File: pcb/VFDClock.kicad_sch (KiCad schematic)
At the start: 32 parts, among them J1 USB_C_Receptacle_USB2.0_16P, SW1 SW_SPST, SW2 SW_SPST, U1 SN74HC595PWR, U2 TBD62783AFWG, U3 TBD62783AFWG, U4 ESP32-S3-WROOM-1, U5 AMS1117-3.3, U6 AMS1117-1.5, U7 AMS1117

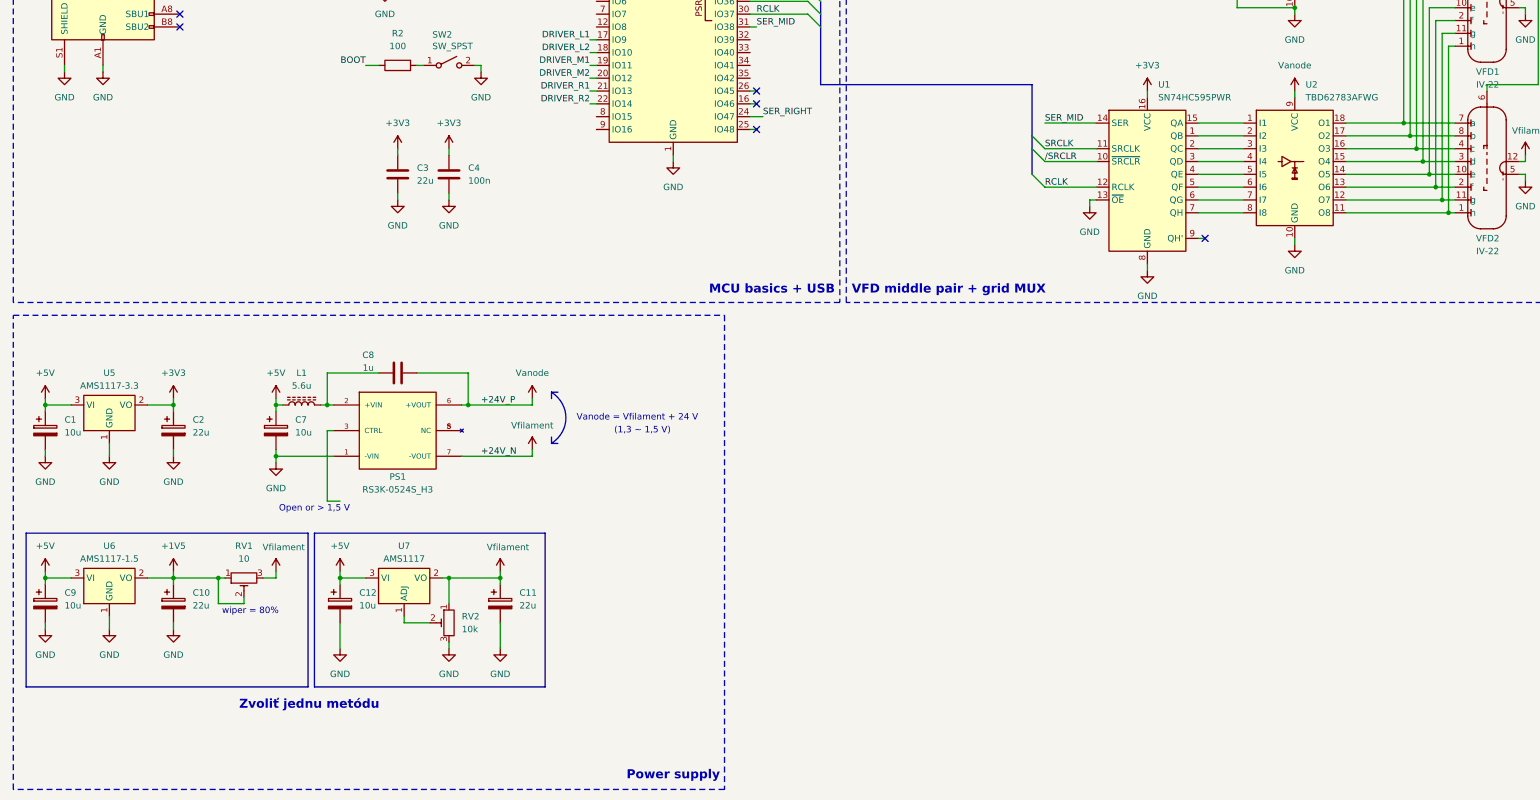
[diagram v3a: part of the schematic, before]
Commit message: Added linear regulator for filament voltage
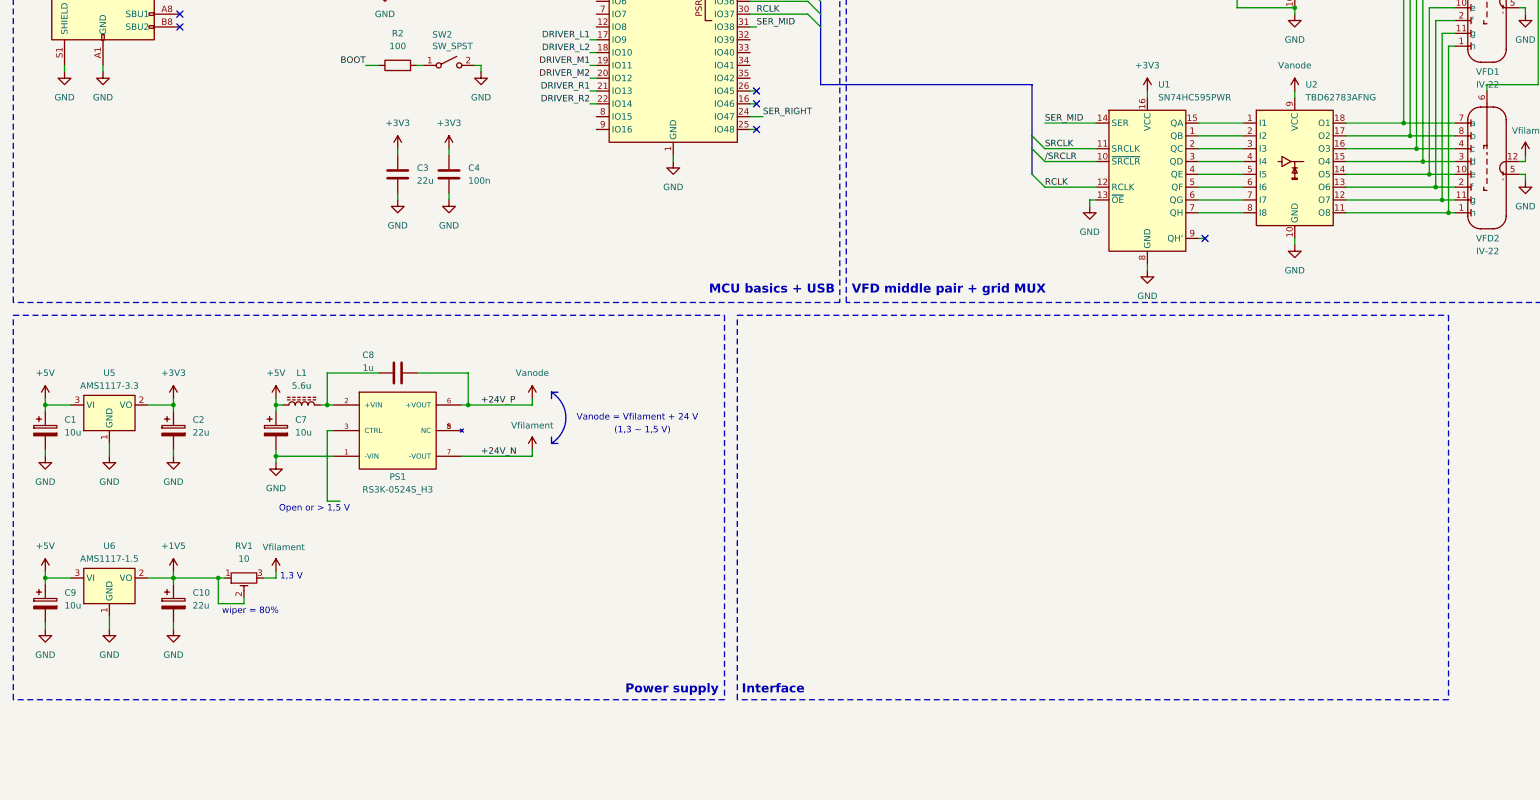
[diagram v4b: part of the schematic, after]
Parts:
- removed C11: 22u, Capacitor_Tantalum_SMD:CP_EIA-3528-15_AVX-H, symbol Device:C_Polarized
- removed C12: 10u, Capacitor_Tantalum_SMD:CP_EIA-3216-18_Kemet-A, symbol Device:C_Polarized
- removed RV2: 10k, symbol Device:R_Potentiometer_Trim
- removed U7: AMS1117, Package_TO_SOT_SMD:SOT-223-3_TabPin2, symbol Regulator_Linear:AMS1117
- J1: footprint Connector_USB:USB_C_Receptacle_GCT_USB4105-xx-A_16P_TopMnt_Horizontal -> Connector_USB:USB_C_Receptacle_GCT_USB4110
- U1: footprint (none) -> Package_SO:TSSOP-16_4.4x5mm_P0.65mm
- U2: value TBD62783AFWG -> TBD62783AFNG; footprint (none) -> Package_SO:SSOP-18_4.4x6.5mm_P0.65mm
- U3: footprint (none) -> Package_SO:SSOP-18_4.4x6.5mm_P0.65mm
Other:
- note added: "1,3 V"
- note added: "Interface"
- note removed: "Zvoliť jednu metódu"

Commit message: Added sensors and general feature ideas
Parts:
- added BT1: Battery_Cell, symbol Device:Battery_Cell
- added D1: Power LED, symbol Device:LED
- added D2: MCU LED, symbol Device:LED
- added D3, D4, D5, D6: Inolux_IN-PI554FCH, LED_SMD:LED_Inolux_IN-PI554FCH_PLCC4_5.0x5.0mm_P3.2mm, symbol LED:Inolux_IN-PI554FCH
- added D7: ESD9B5.0ST5G, Diode_SMD:D_SOD-923, symbol Diode:ESD9B5.0ST5G
- added R10, R9: 1k, Resistor_SMD:R_0805_2012Metric, symbol Device:R
- added R5, R6, R7, R8: 10k, Resistor_SMD:R_0805_2012Metric, symbol Device:R
- added SW3, SW4, SW5, SW6: SW_SPST, symbol Switch:SW_SPST
- added U7: BQ32000, Package_SO:SOIC-8_3.9x4.9mm_P1.27mm, symbol Timer_RTC:BQ32000
- added U8: APDS-9301, OptoDevice:Broadcom_APDS-9301, symbol Sensor_Optical:APDS-9301
- added U9: DHT11, Sensor:Aosong_DHT11_5.5x12.0_P2.54mm, symbol Sensor:DHT11
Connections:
- net +3V3: now also D1.2 (A), D2.2 (A), D3.3 (VDD), D4.3 (VDD), D5.3 (VDD), D6.3 (VDD), R5.1, R6.1, R7.1, R8.1, U7.8 (VCC), U8.1 (VDD), U9.1 (VDD)
- net GND: now also BT1.2 (-), D3.1 (VSS), D4.1 (VSS), D5.1 (VSS), D6.1 (VSS), SW3.2 (B), SW4.2 (B), SW5.2 (B), SW6.2 (B), U7.4 (GND), U8.2 (GND), U8.3 (ADR_SEL), U9.4 (GND)
- net SCL: now reaches U4.10 (IO17)
- net SCL: now also U8.4 (SCL)
- net SDA: now reaches U4.11 (IO18)
- net SDA: now also U8.5 (SDA)
- net BTN4: now reaches U4.12 (IO8)
- net BTN4: now also R8.2, SW6.1 (A)
- net TEMP_DATA: now reaches U4.32 (IO39)
- net TEMP_DATA: now also U9.2 (DATA)
- net LED2: now reaches U4.38 (IO2)
- net LED2: now also R10.2
- net LED1: now reaches U4.39 (IO1)
- net LED1: now also R9.2
- net COLON_LED: now reaches U4.4 (IO4)
- net COLON_LED: now also D5.2 (DIN)
- net BTN1: now reaches U4.5 (IO5)
- net BTN1: now also R5.2, SW3.1 (A)
- net BTN2: now reaches U4.6 (IO6)
- net BTN2: now also R6.2, SW4.1 (A)
- net BTN3: now reaches U4.7 (IO7)
- net BTN3: now also R7.2, SW5.1 (A)
- net RTC_SCL: now reaches U4.8 (IO15)
- net RTC_SCL: now also U7.6 (SCL)
- net RTC_SDA: now reaches U4.9 (IO16)
- net RTC_SDA: now also U7.5 (SDA)
- new net: D5.4 (DO), D6.2 (DIN)
- new net: D1.1 (K), R9.1
- new net: D3.4 (DO), D4.2 (DIN)
- new net: D2.1 (K), R10.1
- new net: D3.2 (DIN), D6.4 (DO)
- new net Vbat: BT1.1 (+), U7.3 (VBACK)
- no-connect marks 10 -> 12
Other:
- note added: "Board interconnect"
- note added: "HH:MM colon"
- note added: "Light sensor"
- note added: "MM:SS colon"
- note added: "Push buttons"
- note added: "RTC"
- note added: "Temperature and humidity sensor"
- note added: "Zapojenie tranzilu Zapojenie neopixleu Konkrétne senzory a RTC Baterka pre RTC Board interconnecty"
- moved on the sheet: C1, C10, C2, C3, C4, C5, C6, C7, C8, C9, J1, L1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

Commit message: Added TVS diodes
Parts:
- removed D7: ESD9B5.0ST5G, Diode_SMD:D_SOD-923, symbol Diode:ESD9B5.0ST5G
- added D1, D2: 36 VB, symbol Device:D_TVS
- added D10, D9: 6 VB, symbol Device:D_TVS
- added D11, D12, D13, D14, D15, D16, D17, D18, D21, D22, D23, D24, D29, D3, D4, D5, D6, D7, D8: 4 VB, symbol Device:D_TVS
- added J1, J2, J4, J5: Conn_02x03_Top_Bottom_MountingPin, symbol Connector_Generic_MountingPin:Conn_02x03_Top_Bottom_MountingPin
- renumbered C3 to C1, C4 to C2, C5 to C3, C6 to C4, C8 to C5, C1 to C6, C2 to C7, C7 to C8, D3 to D19, D4 to D20, D5 to D25, D6 to D26, D1 to D27, D2 to D28, J1 to J3, R3 to R1, R4 to R2, R1 to R3, R2 to R4, SW2 to SW1, SW1 to SW2, U3 to U1, U4 to U2, U2 to U3, U1 to U4, U7 to U6, U6 to U7, U9 to U8, U8 to U9
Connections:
- net +5V: now also J1.1 (Pin_1), J1.2 (Pin_2), J1.3 (Pin_3), J4.1 (Pin_1), J4.2 (Pin_2), J4.3 (Pin_3)
- net BOOT: now also D18.2 (A2)
- net BTN1: now also D21.2 (A2)
- net BTN2: now also D22.2 (A2)
- net BTN3: now also D23.2 (A2)
- net BTN4: now also D24.2 (A2)
- net COLON_LED: now also D29.2 (A2)
- net EN: now also D17.2 (A2)
- net GND: now also D1.2 (A2), D10.1 (A1), D11.1 (A1), D12.1 (A1), D13.1 (A1), D14.1 (A1), D15.1 (A1), D16.1 (A1), D17.1 (A1), D18.1 (A1), D2.2 (A2), D21.1 (A1), D22.1 (A1), D23.1 (A1), D24.1 (A1), D29.1 (A1), D3.1 (A1), D4.1 (A1), D5.1 (A1), D6.1 (A1), D7.1 (A1), D8.1 (A1), D9.1 (A1), J1.4 (Pin_4), J1.5 (Pin_5), J1.6 (Pin_6), J1.MP (MountPin), J2.MP (MountPin), J4.4 (Pin_4), J4.5 (Pin_5), J4.6 (Pin_6), J4.MP (MountPin), J5.MP (MountPin)
- net GRID_L1: now also D3.2 (A2), J2.1 (Pin_1)
- net GRID_L2: now also D4.2 (A2), J2.2 (Pin_2)
- net GRID_R1: now also D11.2 (A2), J5.1 (Pin_1)
- net GRID_R2: now also D12.2 (A2), J5.2 (Pin_2)
- net RCLK: now also D14.2 (A2), D6.2 (A2), J2.6 (Pin_6), J5.6 (Pin_6)
- net SER_LEFT: now also D5.2 (A2), J2.3 (Pin_3)
- net SER_RIGHT: now also D13.2 (A2), J5.3 (Pin_3)
- net SRCLK: now also D16.2 (A2), D8.2 (A2), J2.4 (Pin_4), J5.4 (Pin_4)
- net USB_D_DN: now also D9.2 (A2)
- net USB_D_DP: now also D10.2 (A2)
- net /SRCLR: now also D15.2 (A2), D7.2 (A2), J2.5 (Pin_5), J5.5 (Pin_5)
- net at U1.15 (O4), VFD2.6: now also D2.1 (A1)
- net at U1.16 (O3), VFD1.6: now also D1.1 (A1)
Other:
- note removed: "Vanode"
- note removed: "Vfil"
- note removed: "Vgrid"
- moved on the sheet: BT1, C1, C10, C2, C3, C4, C5, C6, C7, C8, C9, D19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

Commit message: Added TVS and packages for components
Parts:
- removed D1: 36 VB, symbol Device:D_TVS
- removed D10, D9: 6 VB, symbol Device:D_TVS
- removed D11, D12, D13, D14, D15, D16, D17, D18, D21, D22, D23, D24, D29, D4, D5, D6, D7, D8: 4 VB, symbol Device:D_TVS
- added D30, D31, D32, D33, D34, D35: 1PS70SB84, Package_TO_SOT_SMD:SOT-323_SC-70, symbol Diode:BAT54SW
- added U10: IP4234CZ6, Package_TO_SOT_SMD:SC-74-6_1.55x2.9mm_P0.95mm, symbol Power_Protection:IP4234CZ6
- added U11: TXS0101DBV, Package_TO_SOT_SMD:SOT-23-6, symbol Logic_LevelTranslator:TXS0101DBV
- D2: value 36 VB -> XGD10603MR
- D27: footprint (none) -> Diode_SMD:D_0603_1608Metric
- D28: footprint (none) -> LED_SMD:LED_0603_1608Metric
- D3: value 4 VB -> XGD10603MR
- L1: footprint Inductor_SMD:L_0201_0603Metric -> Inductor_SMD:L_1812_4532Metric
- R10, R9: value 1k -> 180
- R4: value 100 -> 10k
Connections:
- net +3V3: now also D30.2 (K), D31.2 (K), D32.2 (K), D33.2 (K), D34.2 (K), D35.2 (K), U11.1 (V_{CCA}), U11.5 (OE); no longer D19.3 (VDD), D20.3 (VDD), D25.3 (VDD), D26.3 (VDD)
- net +5V: now also D19.3 (VDD), D20.3 (VDD), D25.3 (VDD), D26.3 (VDD), U10.5 (VP), U11.6 (V_{CCB})
- net BOOT: now also D35.3 (COM)
- net BTN1: now also D31.3 (COM)
- net BTN2: now also D32.3 (COM)
- net BTN3: now also D33.3 (COM)
- net BTN4: now also D34.3 (COM)
- net COLON_LED: now also U11.3 (A); no longer D25.2 (DIN)
- net EN: now also D30.3 (COM)
- net GND: now also D2.1 (A1), D30.1 (A), D31.1 (A), D32.1 (A), D33.1 (A), D34.1 (A), D35.1 (A), U10.2 (VN), U11.2 (GND); no longer D2.2 (A2)
- net GRID_L1: no longer D3.2 (A2)
- net USB_D_DN: now also U10.4; no longer J3.A7 (D-), J3.B7 (D-)
- net USB_D_DP: now also U10.3; no longer J3.A6 (D+), J3.B6 (D+)
- net at U1.15 (O4), VFD2.6: now also D2.2 (A2); no longer D2.1 (A1)
- net at U1.16 (O3), VFD1.6: now also D3.2 (A2)
- new net: D25.2 (DIN), U11.4 (B)
- new net: J3.A6 (D+), J3.B6 (D+), U10.1
- new net: J3.A7 (D-), J3.B7 (D-), U10.6
- no-connect marks 12 -> 13
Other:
- note added: "5V 3A"
- note added: "Konkrétne senzory a RTC Baterka pre RTC Board interconnecty"
- note added: "LTST-C190GKT"
- note added: "RLS-567"
- note removed: "Open or > 1,5 V"
- note removed: "Power and operation LED"
- note removed: "Vanode = Vdelta + Vfil = 26,5 V"
- note removed: "Vdelta = 25 V"
- note removed: "Vfil = 1,5 V"
- note removed: "Zapojenie tranzilu Zapojenie neopixleu Konkrétne senzory a RTC Baterka pre RTC Board interconnecty"
- moved on the sheet: BT1, C1, C10, C2, C3, C4, C5, C6, C7, C8, C9, D19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

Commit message: Added custom footprints for VEML light sensor, added sensors and RTC, pull-ups for I2C
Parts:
- removed U11: TXS0101DBV, Package_TO_SOT_SMD:SOT-23-6, symbol Logic_LevelTranslator:TXS0101DBV
- removed U6: BQ32000, Package_SO:SOIC-8_3.9x4.9mm_P1.27mm, symbol Timer_RTC:BQ32000
- removed U8: DHT11, Sensor:Aosong_DHT11_5.5x12.0_P2.54mm, symbol Sensor:DHT11
- removed U9: APDS-9301, OptoDevice:Broadcom_APDS-9301, symbol Sensor_Optical:APDS-9301
- added C11: 10u, Capacitor_Tantalum_SMD:CP_EIA-3216-18_Kemet-A, symbol Device:C_Polarized
- added C12, C13, C15, C16: 100n, Capacitor_SMD:C_0805_2012Metric, symbol Device:C
- added C14: 1n, Capacitor_SMD:C_0805_2012Metric, symbol Device:C
- added Q1: BSS138, Package_TO_SOT_SMD:SOT-23, symbol Transistor_FET:BSS138
- added R11, R12, R22: 10k, Resistor_SMD:R_0805_2012Metric, symbol Device:R
- added R13, R14, R15, R16, R17, R18, R19, R20: 4k7, Resistor_SMD:R_0805_2012Metric, symbol Device:R
- added R21: R_Photo, symbol Device:R_Photo
- added U11: DS3231MZ+TRL, Package_SO:SOIC-8_3.9x4.9mm_P1.27mm, symbol Timer_RTC:DS3231MZ
- added U6: SHT45-AD1B-R2, Sensor_Humidity:Sensirion_DFN-4_1.5x1.5mm_P0.8mm_SHT4x_NoCentralPad, symbol Sensor_Humidity:SHT4x
- added U8: VEML3235SL, VFDClock_custom_lib:VEML3235SL_Vertical, symbol VFDClock_custom_lib:VEML3235SL
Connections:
- net +3V3: now also C11.1, C12.1, C13.1, C16.1, Q1.1 (G), R11.1, R13.1, R14.1, R15.1, R16.1, R17.1, R18.1, R19.1, R20.1, R21.1, U11.6 (VBAT), U6.3 (VDD), U8.1 (VDD)
- net +5V: now also R12.1
- net COLON_LED: now also Q1.2 (S), R11.2
- net GND: now also C11.2, C12.2, C13.2, C14.2, C15.2, C16.2, R22.2, U11.5 (GND), U6.4 (VSS), U8.2 (GND)
- net SCL: now also R13.2, R15.2, R17.2, R19.2, U11.8 (SCL), U6.2 (SCL), U8.3 (SDA)
- net SDA: now also R14.2, R16.2, R18.2, R20.2, U11.7 (SDA), U6.1 (SDA), U8.4 (SCL)
- net Vbat: now also C14.1, C15.1, U11.2 (VCC)
- net at D25.2 (DIN): now also Q1.3 (D), R12.2
- net RTC_SCL: no longer names the net of U2.8 (IO15)
- net RTC_SDA: no longer names the net of U2.9 (IO16)
- new net Uphoto: R21.2, R22.1
- no-connect marks 13 -> 16
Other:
- note added: "I/O"
- note added: "LIGHT SENS"
- note added: "Level shifter"
- note added: "MCU"
- note added: "Power budget na 3V3 Board interconnecty"
- note added: "Recommended debounce"
- note added: "TEMP SENS"
- note removed: "Interface"
- note removed: "Konkrétne senzory a RTC Baterka pre RTC Board interconnecty"
- moved on the sheet: C3, C4, D19, D20, D25, D26, D27, D28, D30, D31, D32, D33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
